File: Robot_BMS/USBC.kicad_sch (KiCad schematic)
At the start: 2 parts, among them IC2 STUSB4710AQTR, P1 USB_C_Plug

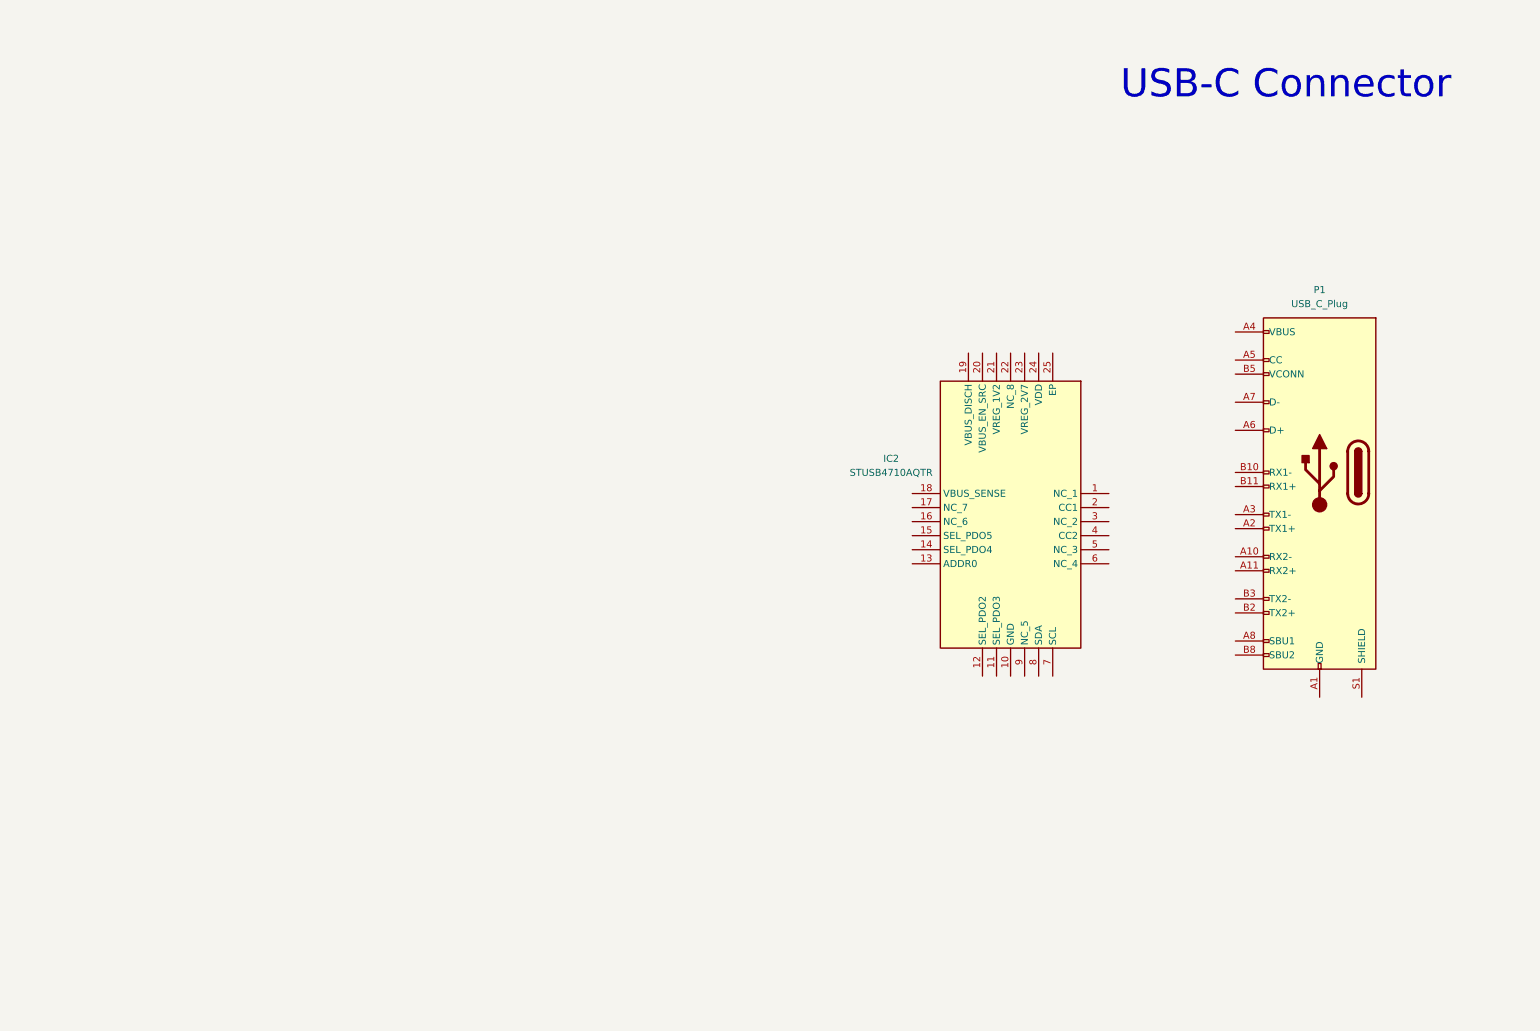
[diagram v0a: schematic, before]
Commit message: DC power supply added via dc Barrel jack
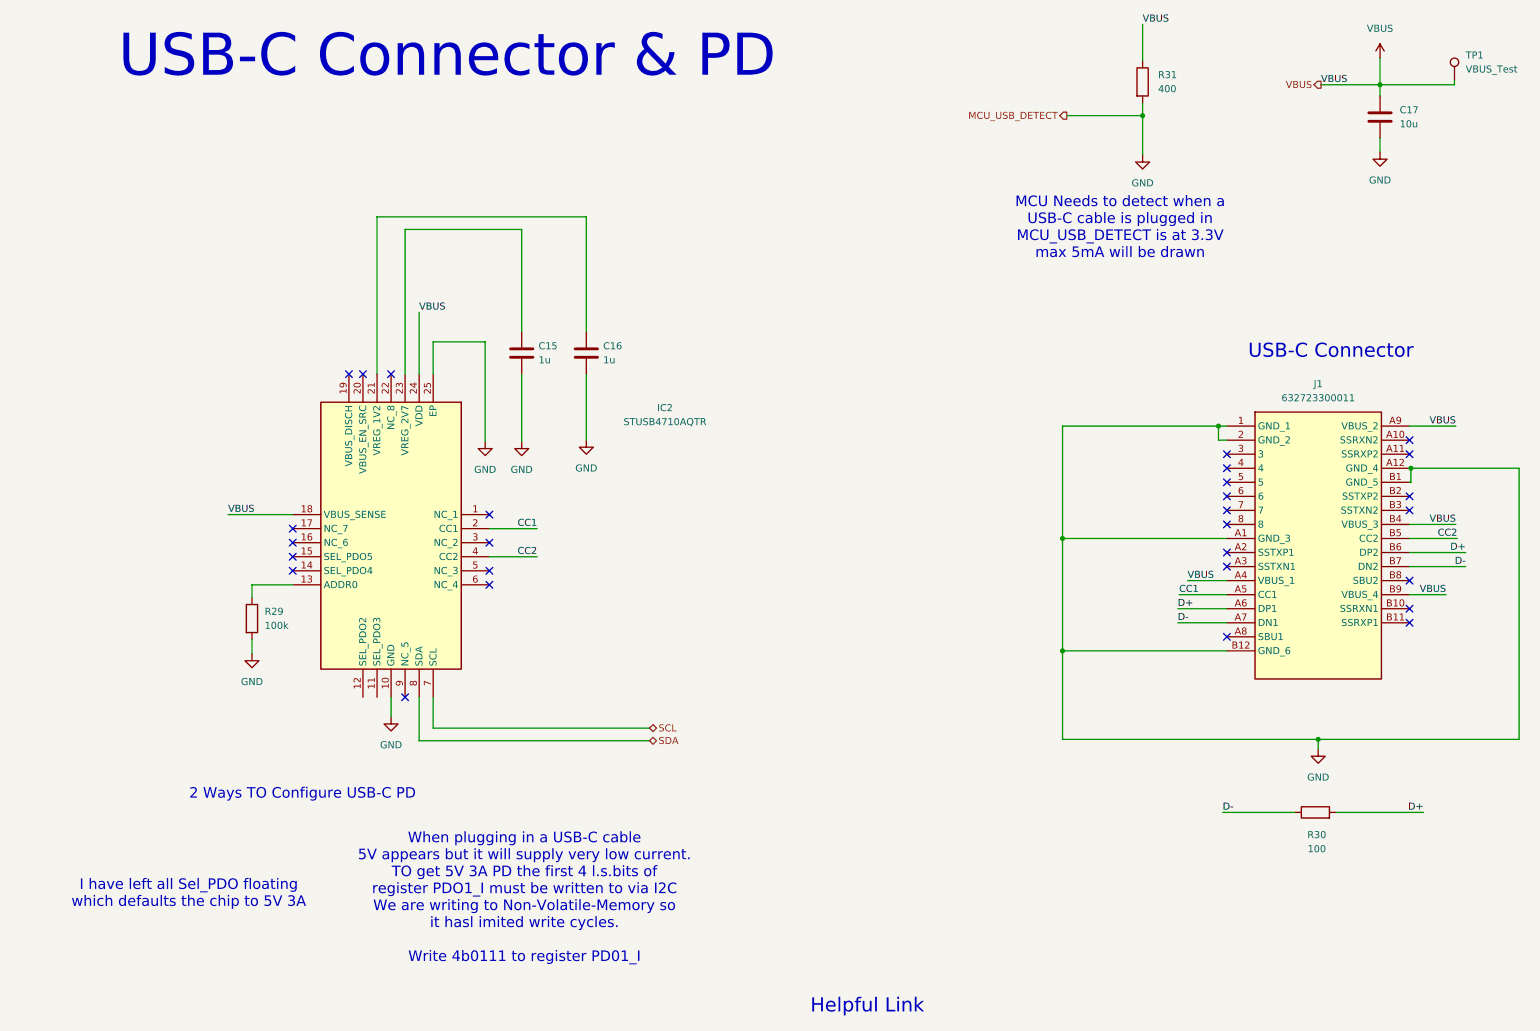
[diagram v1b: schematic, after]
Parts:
- removed P1: USB_C_Plug, symbol Connector:USB_C_Plug
- added C15, C16: 1u, symbol Device:C
- added C17: 10u, symbol Device:C
- added J1: 632723300011, 632723300011, symbol USB-C Connector 632723300011:632723300011
- added R29: 100k, symbol Device:R
- added R30: 100, symbol Device:R
- added R31: 400, symbol Device:R
- added TP1: VBUS_Test, TestPoint:TestPoint_Pad_D4.0mm, symbol Connector:TestPoint
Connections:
- net GND: now reaches IC2.10 (GND)
- net GND: now also IC2.25 (EP), C15.2, C16.2, C17.2, J1.1 (GND_1), J1.2 (GND_2), J1.A1 (GND_3), J1.A12 (GND_4), J1.B1 (GND_5), J1.B12 (GND_6), R29.2, R31.2
- net at IC2.13 (ADDR0): now also R29.1
- net VBUS: now reaches IC2.18 (VBUS_SENSE)
- net VBUS: now also IC2.24 (VDD), C17.1, J1.A4 (VBUS_1), J1.A9 (VBUS_2), J1.B4 (VBUS_3), J1.B9 (VBUS_4), R31.1, TP1.1
- net CC1: now reaches IC2.2 (CC1)
- net CC1: now also J1.A5 (CC1)
- net at IC2.21 (VREG_1V2): now also C16.1
- net at IC2.23 (VREG_2V7): now also C15.1
- net CC2: now reaches IC2.4 (CC2)
- net CC2: now also J1.B5 (CC2)
- net SCL: now reaches IC2.7 (SCL)
- net SDA: now reaches IC2.8 (SDA)
- new net D+: J1.A6 (DP1), J1.B6 (DP2), R30.2
- new net D-: J1.A7 (DN1), J1.B7 (DN2), R30.1
- no-connect marks 0 -> 28
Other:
- note added: "2 Ways TO Configure USB-C PD"
- note added: "Helpful Link"
- note added: "I have left all Sel_PDO floating which defaults the chip to 5V 3A"
- note added: "MCU Needs to detect when a USB-C cable is plugged in MCU_USB_DETECT is at 3.3V max 5mA will be drawn"
- note added: "USB-C Connector & PD"
- note added: "When plugging in a USB-C cable 5V appears but it will supply very low current. TO get 5V 3A PD the first 4 l.s.bits of register PDO1_I must be written to via I2C We are writing to Non-Volatile-Memory so it hasl imited write cycles. Write 4b0111 to register PD01_I"
- moved on the sheet: IC2

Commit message: implementing sepic converter for Solar power input
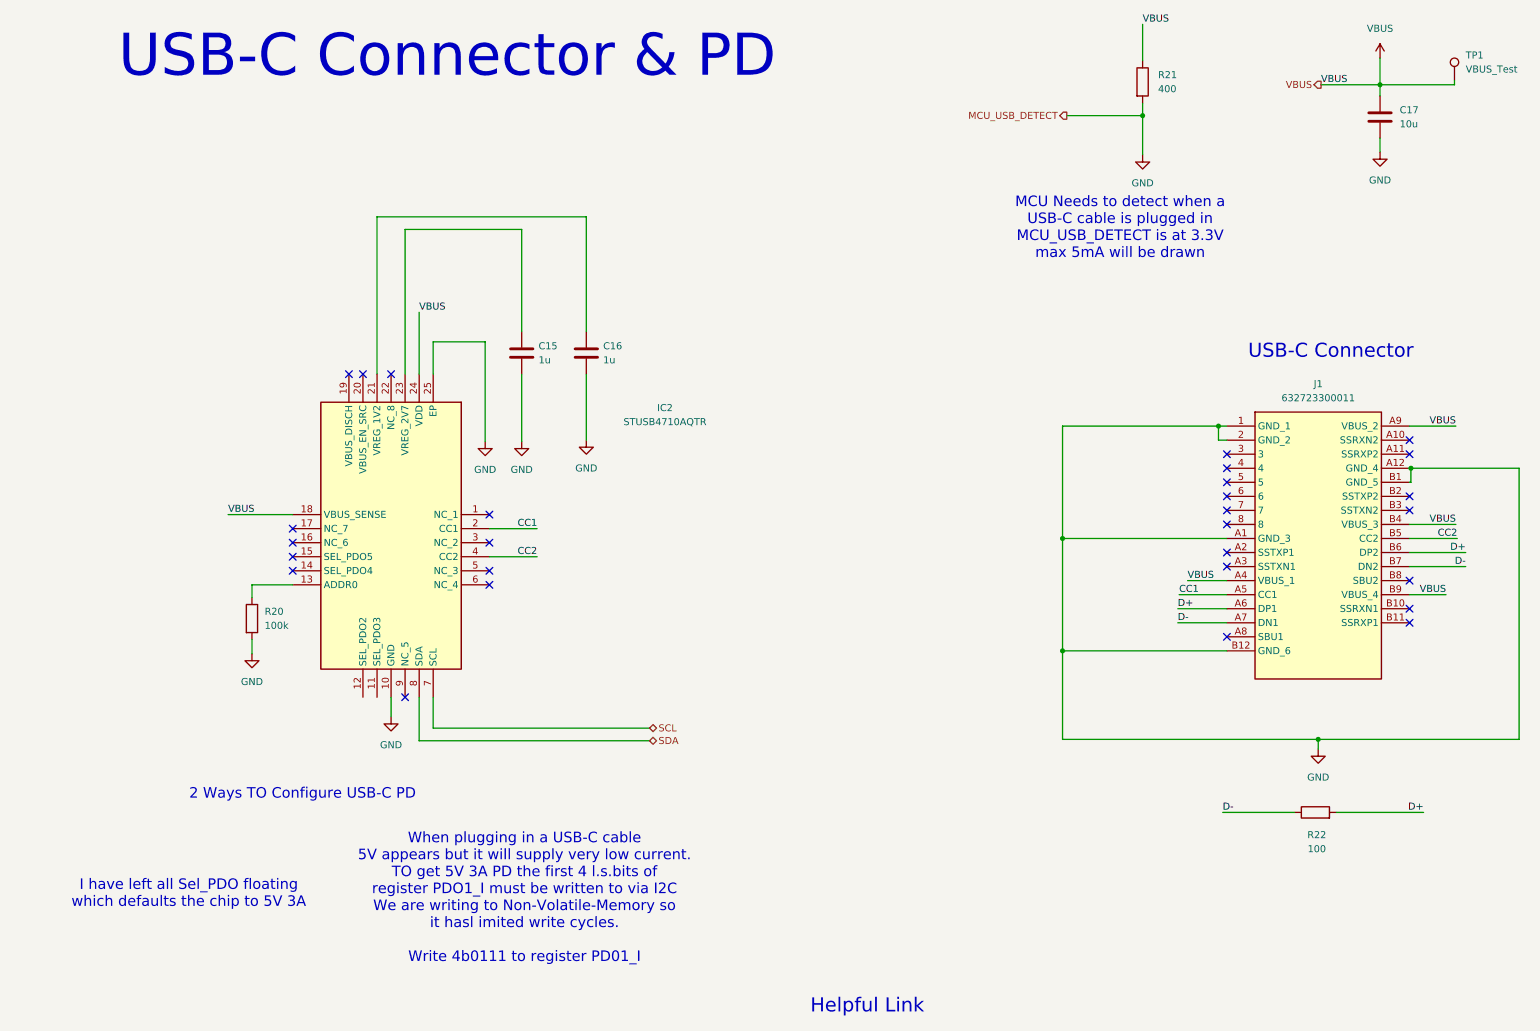
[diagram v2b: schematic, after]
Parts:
- renumbered R29 to R20, R31 to R21, R30 to R22
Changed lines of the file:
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@@
 		(dnp no)
 		(fields_autoplaced yes)
-		(property "Reference" "#PWR019"
+		(property "Reference" "#PWR011"
 			(at 94.234 98.552 0)
 			(effects
@@
 			(project "Robot_BMS"
 				(path "/72551b1c-3d40-4199-8911-e5b015f4abec/c1bdabe1-a4b5-470d-80f8-90d5658c2a45"
-					(reference "#PWR019")
+					(reference "#PWR011")
 					(unit 1)
 				)
@@
 		(dnp no)
 		(fields_autoplaced yes)
-		(property "Reference" "#PWR016"
+		(property "Reference" "#PWR09"
 			(at 52.07 136.906 0)
 			(effects
@@
 			(project "Robot_BMS"
 				(path "/72551b1c-3d40-4199-8911-e5b015f4abec/c1bdabe1-a4b5-470d-80f8-90d5658c2a45"
-					(reference "#PWR016")
+					(reference "#PWR09")
 					(unit 1)
 				)
@@
 		(dnp no)
 		(fields_autoplaced yes)
-		(property "Reference" "#PWR017"
+		(property "Reference" "#PWR013"
 			(at 112.522 98.298 0)
 			(effects
@@
 			(project "Robot_BMS"
 				(path "/72551b1c-3d40-4199-8911-e5b015f4abec/c1bdabe1-a4b5-470d-80f8-90d5658c2a45"
-					(reference "#PWR017")
+					(reference "#PWR013")
 					(unit 1)
 				)
@@
 		(dnp no)
 		(fields_autoplaced yes)
-		(property "Reference" "#PWR013"
+		(property "Reference" "#PWR010"
 			(at 77.216 148.336 0)
 			(effects
@@
 			(project "Robot_BMS"
 				(path "/72551b1c-3d40-4199-8911-e5b015f4abec/c1bdabe1-a4b5-470d-80f8-90d5658c2a45"
-					(reference "#PWR013")
+					(reference "#PWR010")
 					(unit 1)
 				)
@@
 		(dnp no)
 		(fields_autoplaced yes)
-		(property "Reference" "#PWR015"
+		(property "Reference" "#PWR017"
 			(at 256.032 46.228 0)
 			(effects
@@
 			(project "Robot_BMS"
 				(path "/72551b1c-3d40-4199-8911-e5b015f4abec/c1bdabe1-a4b5-470d-80f8-90d5658c2a45"
-					(reference "#PWR015")
+					(reference "#PWR017")
 					(unit 1)
 				)
@@
 		(dnp no)
 		(fields_autoplaced yes)
-		(property "Reference" "R31"
+		(property "Reference" "R21"
 			(at 215.9 25.9079 0)
 			(effects
@@
 			(project ""
 				(path "/72551b1c-3d40-4199-8911-e5b015f4abec/c1bdabe1-a4b5-470d-80f8-90d5658c2a45"
-					(reference "R31")
+					(reference "R21")
 					(unit 1)
 				)
@@
 		(dnp no)
 		(fields_autoplaced yes)
-		(property "Reference" "#PWR014"
+		(property "Reference" "#PWR012"
 			(at 100.838 98.552 0)
 			(effects
@@
 			(project "Robot_BMS"
 				(path "/72551b1c-3d40-4199-8911-e5b015f4abec/c1bdabe1-a4b5-470d-80f8-90d5658c2a45"
-					(reference "#PWR014")
+					(reference "#PWR012")
 					(unit 1)
 				)
@@
 		(dnp no)
 		(fields_autoplaced yes)
-		(property "Reference" "R29"
+		(property "Reference" "R20"
 			(at 54.356 122.9359 0)
 			(effects
@@
 			(project ""
 				(path "/72551b1c-3d40-4199-8911-e5b015f4abec/c1bdabe1-a4b5-470d-80f8-90d5658c2a45"
-					(reference "R29")
+					(reference "R20")
 					(unit 1)
 				)
@@
 		(dnp no)
 		(fields_autoplaced yes)
-		(property "Reference" "#PWR011"
+		(property "Reference" "#PWR015"
 			(at 244.856 154.178 0)
 			(effects
@@
 			(project "Robot_BMS"
 				(path "/72551b1c-3d40-4199-8911-e5b015f4abec/c1bdabe1-a4b5-470d-80f8-90d5658c2a45"
-					(reference "#PWR011")
+					(reference "#PWR015")
 					(unit 1)
 				)
@@
 		(dnp no)
 		(fields_autoplaced yes)
-		(property "Reference" "#PWR012"
+		(property "Reference" "#PWR016"
 			(at 256.032 26.67 0)
 			(effects
@@
 			(project ""
 				(path "/72551b1c-3d40-4199-8911-e5b015f4abec/c1bdabe1-a4b5-470d-80f8-90d5658c2a45"
-					(reference "#PWR012")
+					(reference "#PWR016")
 					(unit 1)
 				)
@@
 		(on_board yes)
 		(dnp no)
-		(property "Reference" "R30"
+		(property "Reference" "R22"
 			(at 244.602 163.322 90)
 			(effects
@@
 			(project ""
 				(path "/72551b1c-3d40-4199-8911-e5b015f4abec/c1bdabe1-a4b5-470d-80f8-90d5658c2a45"
-					(reference "R30")
+					(reference "R22")
 					(unit 1)
 				)
@@
 		(dnp no)
 		(fields_autoplaced yes)
-		(property "Reference" "#PWR018"
+		(property "Reference" "#PWR014"
 			(at 213.106 46.736 0)
 			(effects
@@
 			(project "Robot_BMS"
 				(path "/72551b1c-3d40-4199-8911-e5b015f4abec/c1bdabe1-a4b5-470d-80f8-90d5658c2a45"
-					(reference "#PWR018")
-					(unit 1)
-				)
+					(reference "#PWR014")
+					(unit 1)
+				)

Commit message: USB-c PD to 15V
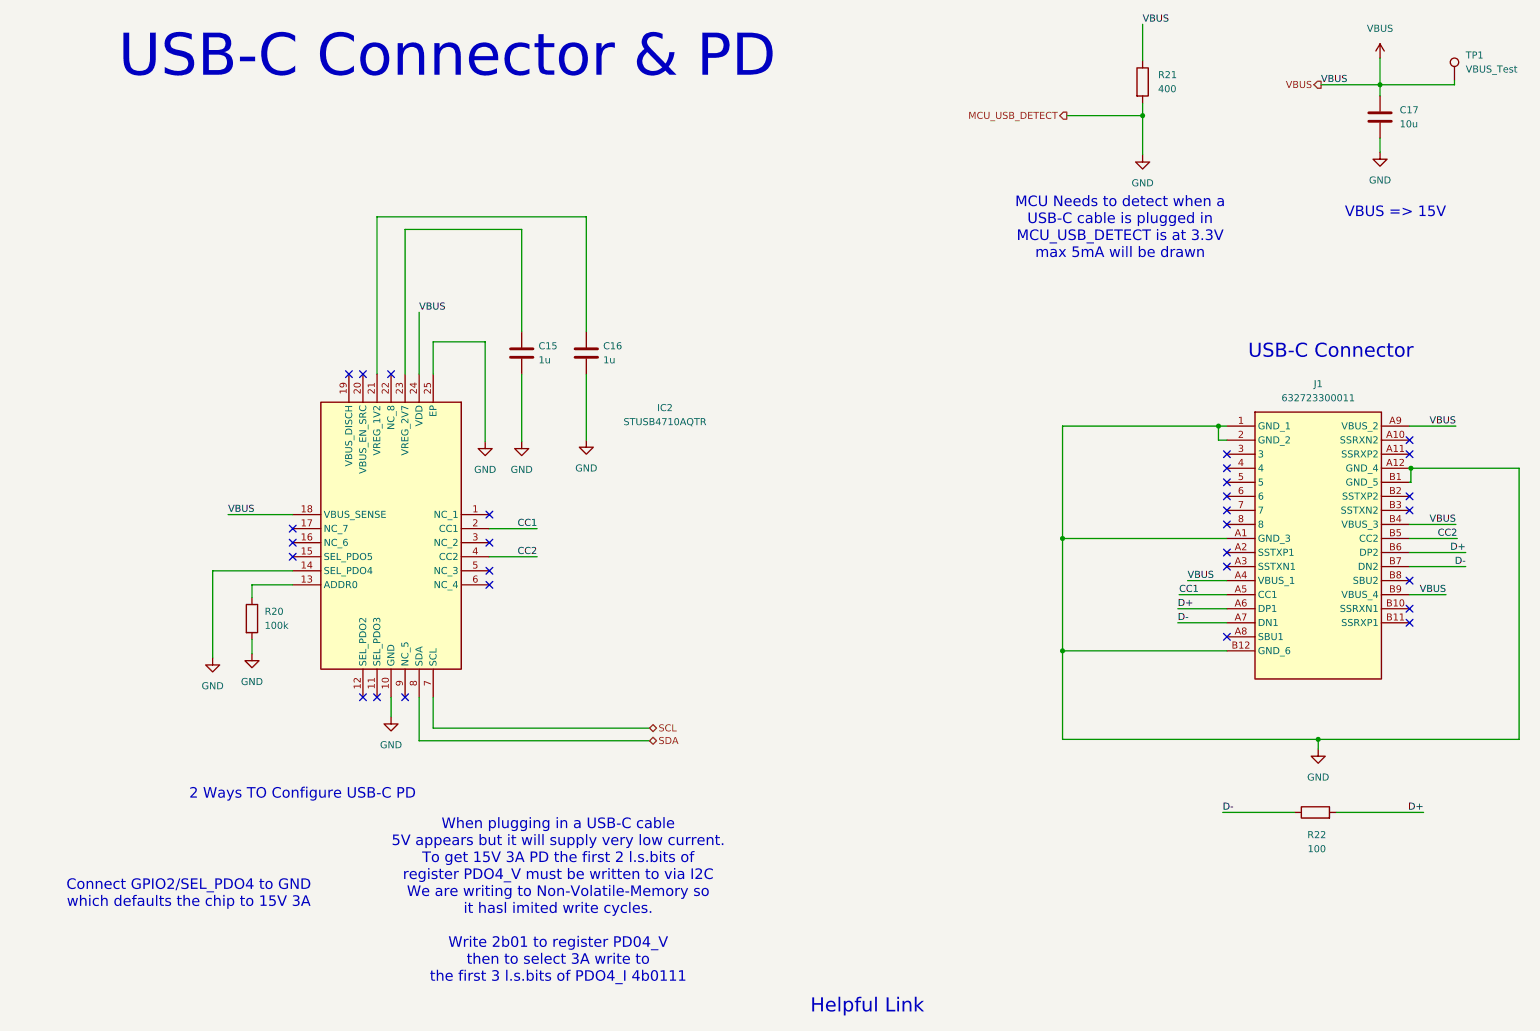
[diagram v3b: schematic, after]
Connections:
- net GND: now also IC2.14 (SEL_PDO4)
- no-connect marks 28 -> 29
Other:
- note added: "Connect GPIO2/SEL_PDO4 to GND which defaults the chip to 15V 3A"
- note added: "VBUS => 15V"
- note added: "When plugging in a USB-C cable 5V appears but it will supply very low current. To get 15V 3A PD the first 2 l.s.bits of register PDO4_V must be written to via I2C We are writing to Non-Volatile-Memory so it hasl imited write cycles. Write 2b01 to register PD04_V then to select 3A write to the first 3 l.s.bits of PDO4_I 4b0111"
- note removed: "I have left all Sel_PDO floating which defaults the chip to 5V 3A"
- note removed: "When plugging in a USB-C cable 5V appears but it will supply very low current. TO get 5V 3A PD the first 4 l.s.bits of register PDO1_I must be written to via I2C We are writing to Non-Volatile-Memory so it hasl imited write cycles. Write 4b0111 to register PD01_I"
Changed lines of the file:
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@@
+	)
+	(no_connect
+		(at 74.676 138.43)
 	)
 	(no_connect
@@
 	)
 	(no_connect
+		(at 72.136 138.43)
+	)
+	(no_connect
 		(at 94.996 115.57)
 	)
@@
 	)
 	(no_connect
-		(at 59.436 115.57)
-	)
-	(no_connect
 		(at 59.436 113.03)
 	)
@@
 	(wire
 		(pts
+			(xy 44.958 115.57) (xy 59.436 115.57)
+		)
+		(stroke
+			(width 0)
+			(type default)
+		)
+	)
+	(wire
+		(pts
 			(xy 82.296 68.834) (xy 82.296 80.01)
 		)
@@
 		(pts
 			(xy 112.522 51.562) (xy 112.522 72.39)
+		)
+		(stroke
+			(width 0)
+			(type default)
+		)
+	)
+	(wire
+		(pts
+			(xy 44.958 131.318) (xy 44.958 115.57)
 		)
 		(stroke
@@
 		)
 	)
-	(text "When plugging in a USB-C cable \n5V appears but it will supply very low current.\nTO get 5V 3A PD the first 4 l.s.bits of\nregister PDO1_I must be written to via I2C\nWe are writing to Non-Volatile-Memory so \nit hasl imited write cycles.\n\nWrite 4b0111 to register PD01_I"
+	(text "When plugging in a USB-C cable \n5V appears but it will supply very low current.\nTo get 15V 3A PD the first 2 l.s.bits of\nregister PDO4_V must be written to via I2C\nWe are writing to Non-Volatile-Memory so \nit hasl imited write cycles.\n\nWrite 2b01 to register PD04_V\nthen to select 3A write to\nthe first 3 l.s.bits of PDO4_I 4b0111"
 		(exclude_from_sim no)
-		(at 101.346 174.752 0)
+		(at 107.442 175.26 0)
+		(effects
+			(font
+				(size 1.905 1.905)
+			)
+		)
+	)
+	(text "VBUS => 15V"
+		(exclude_from_sim no)
+		(at 258.826 50.8 0)
 		(effects
 			(font
@@
 		)
 	)
-	(text "I have left all Sel_PDO floating \nwhich defaults the chip to 5V 3A"
+	(text "Connect GPIO2/SEL_PDO4 to GND\nwhich defaults the chip to 15V 3A"
 		(exclude_from_sim no)
 		(at 40.64 173.99 0)
@@
 					(unit 1)
 				)
+			)
+		)
+	)
+	(symbol
+		(lib_id "power:GND")
+		(at 44.958 131.318 0)
+		(unit 1)
+		(exclude_from_sim no)
+		(in_bom yes)
+		(on_board yes)
+		(dnp no)
+		(fields_autoplaced yes)
+		(property "Reference" "#PWR035"
+			(at 44.958 137.668 0)
+			(effects
+				(font
+					(size 1.27 1.27)
+				)
+				(hide yes)
+			)
+		)
+		(property "Value" "GND"
+			(at 44.958 136.398 0)
+			(effects
+				(font
+					(size 1.27 1.27)
+				)
+			)
+		)
+		(property "Footprint" ""
+			(at 44.958 131.318 0)
+			(effects
+				(font
+					(size 1.27 1.27)
+				)
+				(hide yes)
+			)
+		)
+		(property "Datasheet" ""
+			(at 44.958 131.318 0)
+			(effects
+				(font
+					(size 1.27 1.27)
+				)
+				(hide yes)
+			)
+		)
+		(property "Description" "Power symbol creates a global label with name \"GND\" , ground"
+			(at 44.958 131.318 0)
+			(effects
+				(font
+					(size 1.27 1.27)
+				)
+				(hide yes)
+			)
+		)
+		(pin "1"
+		)
+		(instances
+			(project "Robot_BMS"
+				(path "/72551b1c-3d40-4199-8911-e5b015f4abec/c1bdabe1-a4b5-470d-80f8-90d5658c2a45"
+					(reference "#PWR035")
+					(unit 1)
+				)
